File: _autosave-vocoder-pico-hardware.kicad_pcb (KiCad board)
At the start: 2 copper layers, 76 parts, among them J1 Conn_02x05_Odd_Even, J2 AudioJack2_SwitchT, J2 AudioJack3_SwitchTR, J3 AudioJack3_SwitchTR, J4 AudioJack2_SwitchT, Q1 BC547, Q2 BC547, Q3 BC547, Q4 BC547, SW1 SW_Push, SW2 SW_Push, U1 TL072, U2 LM7805_TO220, U3 PCM5100A, U4 SC39-11GWA, U5 SC39-11GWA, U6 SC39-11GWA, U7 SC39-11GWA, U8 MCP6002-xP, U9 TL072

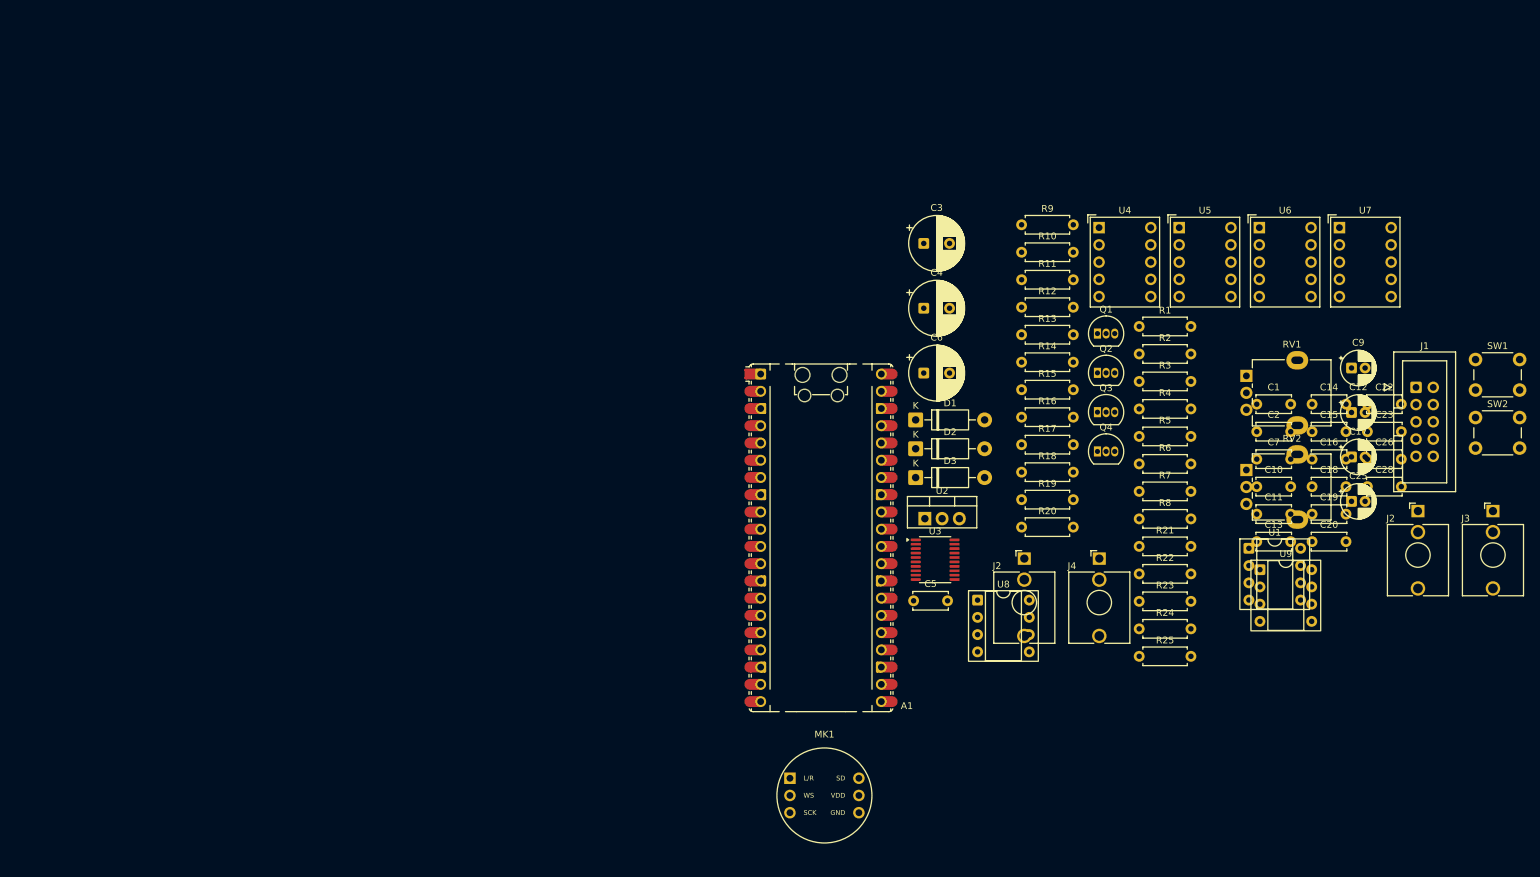
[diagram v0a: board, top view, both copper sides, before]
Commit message: fix wrong symbol
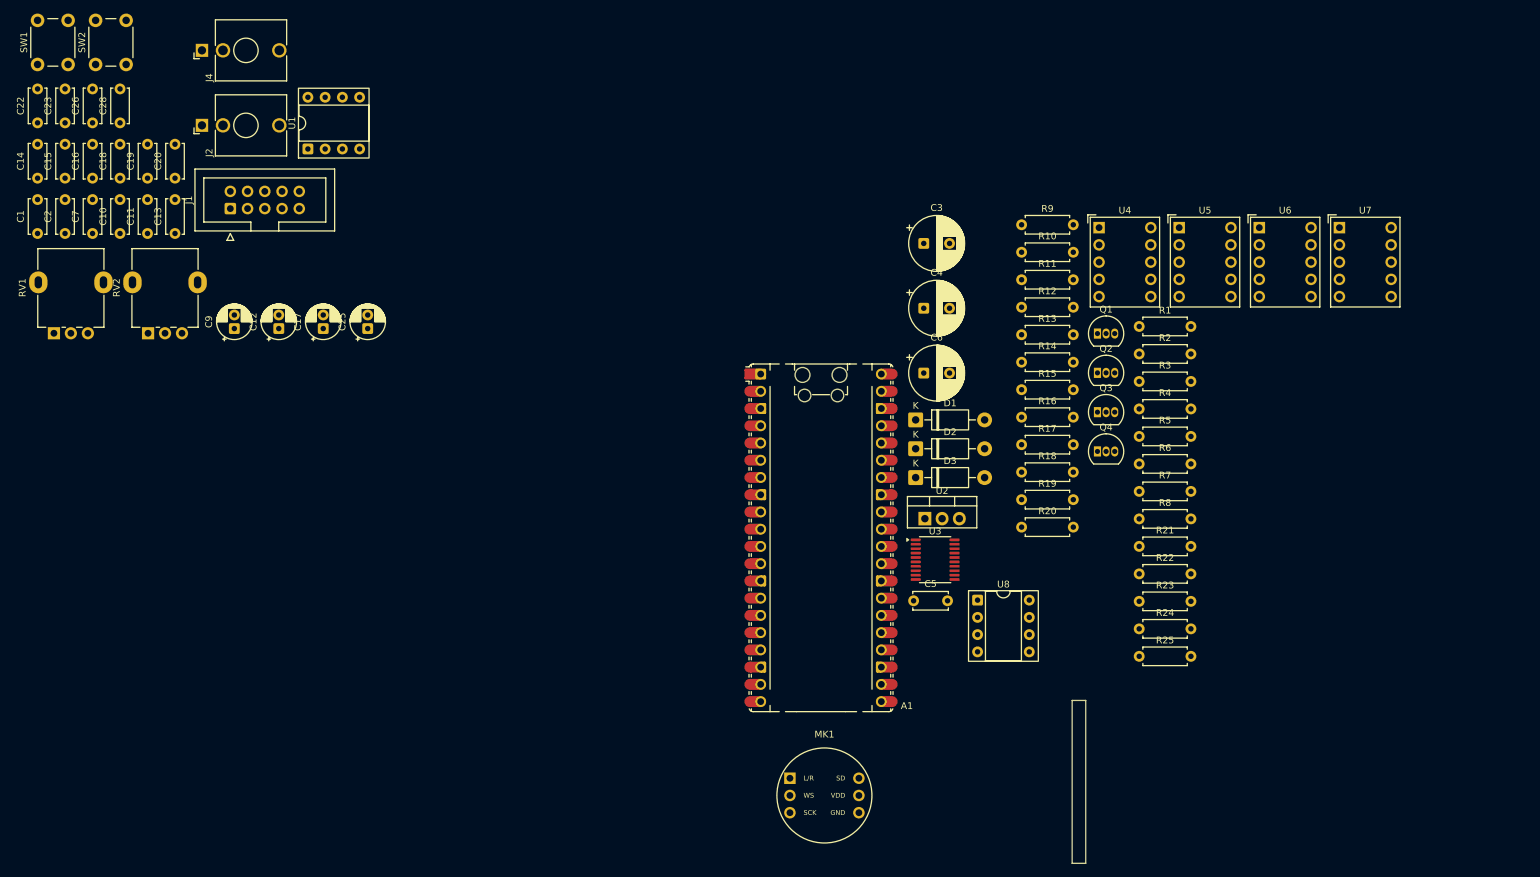
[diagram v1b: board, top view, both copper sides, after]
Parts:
- removed the J2 at (144.9, 82.1)
- removed the J2 at (202.9, 75.1)
- removed J3: AudioJack3_SwitchTR, Connector_Audio:Jack_3.5mm_QingPu_WQP-PJ398SM_Vertical_CircularHoles
- removed U9: TL072, Package_DIP:DIP-8_W7.62mm_Socket
- added J2: AudioJack2_SwitchT, Connector_Audio:Jack_3.5mm_QingPu_WQP-PJ398SM_Vertical_CircularHoles, F.Cu at (23.8, 18.3)
- U8: value MCP6002-xP -> Amplifier_Operational:MCP6002-xP
- moved SW1 216.3 mm to (-0.43, 9.30), turned to 90 degrees
- moved SW2 209.9 mm to (8.12, 9.30), turned to 90 degrees
- moved C22 200.3 mm to (-0.43, 17.9), turned to 90 degrees
- moved C23 197.2 mm to (3.62, 17.9), turned to 90 degrees
- moved C26 194.3 mm to (7.67, 17.9), turned to 90 degrees
- moved C28 191.4 mm to (11.7, 17.9), turned to 90 degrees
- moved C14 190.7 mm to (-0.43, 26.1), turned to 90 degrees
- moved C15 187.5 mm to (3.62, 26.1), turned to 90 degrees
- moved C16 184.4 mm to (7.67, 26.1), turned to 90 degrees
- moved C18 181.4 mm to (11.7, 26.1), turned to 90 degrees
- moved C1 181.4 mm to (-0.43, 34.2), turned to 90 degrees
- moved C19 178.6 mm to (15.8, 26.1), turned to 90 degrees
- moved C2 178.0 mm to (3.62, 34.2), turned to 90 degrees
- moved J1 176.7 mm to (28.0, 30.5), turned to 90 degrees
- moved C20 175.9 mm to (19.8, 26.1), turned to 90 degrees
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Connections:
- U1 pad 5: (no net) -> GND
- U1 pad 6: (no net) -> Net-(U1B--)
- U1 pad 7: (no net) -> Net-(U1B--)
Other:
- board outline added: 2 x 24 mm

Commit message: run erc checks and added fixes
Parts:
- removed the J2 at (23.8, 18.3)
- removed the U1 at (39.4, 21.8)
- added J2: AudioJack2_SwitchT, Connector_Audio:Jack_3.5mm_QingPu_WQP-PJ398SM_Vertical_CircularHoles, F.Cu at (144.9, 82.1)
- added J2: AudioJack3_SwitchTR, Connector_Audio:Jack_3.5mm_QingPu_WQP-PJ398SM_Vertical_CircularHoles, F.Cu at (202.9, 75.1)
- added J3: AudioJack3_SwitchTR, Connector_Audio:Jack_3.5mm_QingPu_WQP-PJ398SM_Vertical_CircularHoles, F.Cu at (214.0, 75.1)
- added U1: TL072, Package_DIP:DIP-8_W7.62mm_Socket, F.Cu at (178.0, 80.6)
- added U1: TL072, Package_DIP:DIP-8_W7.62mm_Socket, F.Cu at (179.7, 83.7)
- U8: value Amplifier_Operational:MCP6002-xP -> MCP6002-xP
- moved SW1 216.3 mm to (211.4, 52.8), turned to 0 degrees
- moved SW2 209.9 mm to (211.4, 61.3), turned to 0 degrees
- moved C22 200.3 mm to (195.5, 59.4), turned to 0 degrees
- moved C23 197.2 mm to (195.5, 63.4), turned to 0 degrees
- moved C26 194.3 mm to (195.5, 67.5), turned to 0 degrees
- moved C28 191.4 mm to (195.5, 71.5), turned to 0 degrees
- moved C14 190.7 mm to (187.3, 59.4), turned to 0 degrees
- moved C15 187.5 mm to (187.3, 63.4), turned to 0 degrees
- moved C16 184.4 mm to (187.3, 67.5), turned to 0 degrees
- moved C18 181.4 mm to (187.3, 71.5), turned to 0 degrees
- moved C1 181.4 mm to (179.2, 59.4), turned to 0 degrees
- moved C19 178.6 mm to (187.3, 75.5), turned to 0 degrees
- moved C2 178.0 mm to (179.2, 63.4), turned to 0 degrees
- moved J1 176.7 mm to (202.7, 56.9), turned to 0 degrees
- moved C20 175.9 mm to (187.3, 79.6), turned to 0 degrees
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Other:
- board outline removed
